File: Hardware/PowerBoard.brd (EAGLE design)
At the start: 97 x 38.1 mm, 32 parts, among them IC1 MAX232, IC2 7805

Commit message: Added HV supply; cleaned up power board
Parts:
- removed C1: 2.2µF, rcl:C0805
- removed C7: 100nF, rcl:C0805
- added C104: 2.2µF, rcl:C0805
- added C106: 100nF, rcl:C0805
- renumbered C10 to C207, C12 to C202, C13 to C206, C2 to C103, C24 to C203, C25 to C204, C26 to C201, C3 to C105, C4 to C107, C5 to C101, C6 to C102, C8 to C205, H1 to H101, H2 to H102, H3 to H103, IC1 to IC101, IC2 to IC201, LED1 to LED201, LED5 to LED202, R1 to R201, R13 to R202, S2 to S101, SV1 to SV202, SV2 to SV203, SV3 to SV204, SV5 to SV101, SV6 to SV102, SV7 to SV201, X1 to X101, X2 to X102
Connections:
- net +5V: now also C106.1; no longer C7.1
- net GND: now also C104.2, C106.2; no longer C1.2, C7.2
- net N$1: now also C104.1; no longer C1.1
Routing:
- net +5V: track 159.9 -> 161.3 mm
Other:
- board text added: "UART/Power Board Rev 01"

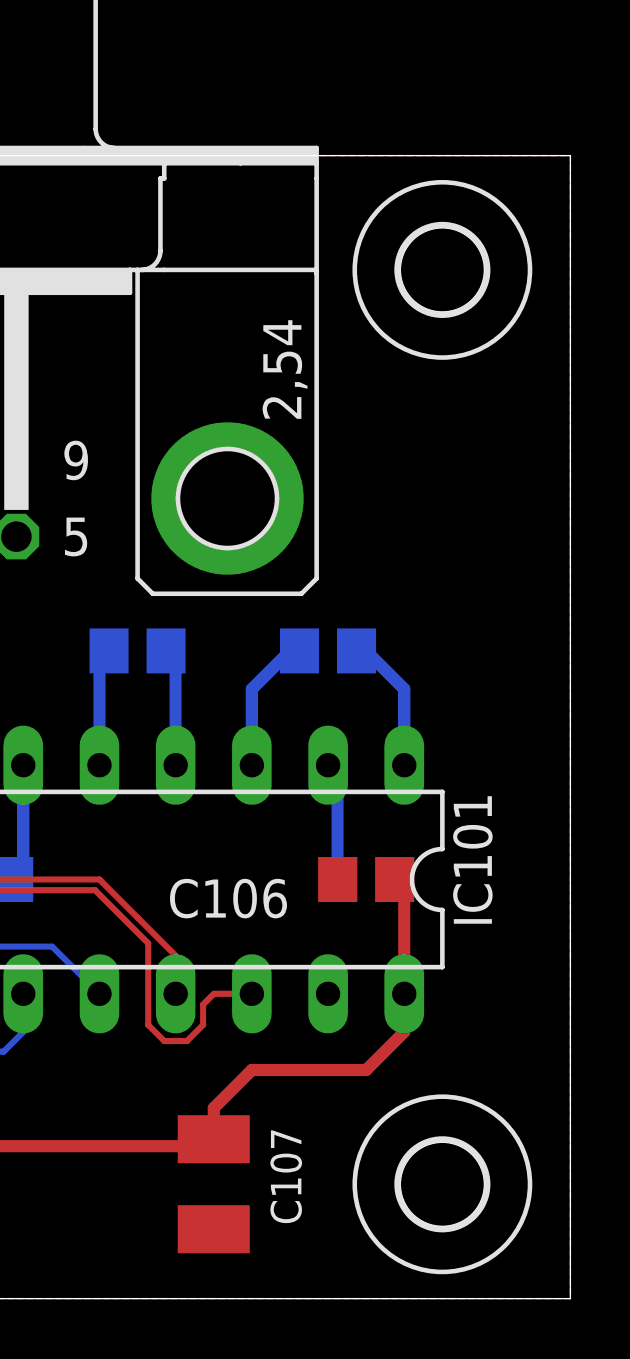
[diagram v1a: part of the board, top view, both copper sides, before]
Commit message: added ARM chip to driver boards to PWM tubes
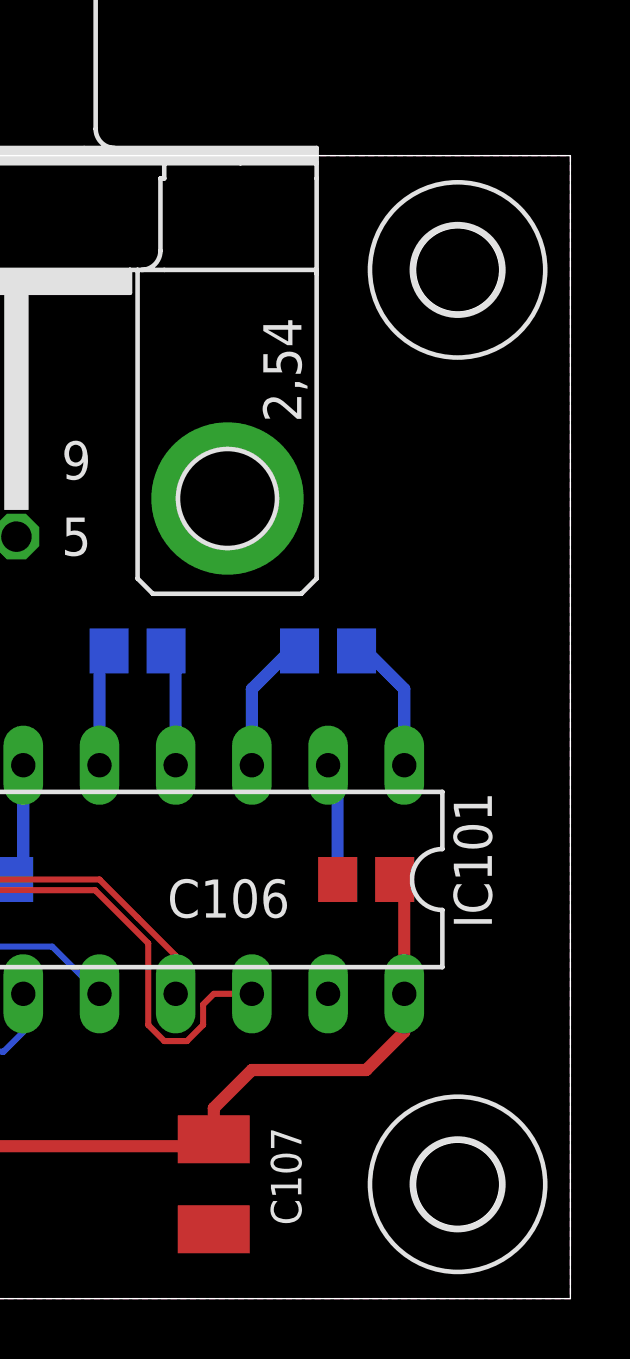
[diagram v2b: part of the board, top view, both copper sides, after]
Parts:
- moved H102 0.51 mm to (93.2, 34.3)
- moved H103 0.51 mm to (93.2, 3.81)
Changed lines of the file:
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@@
 </class>
 </classes>
-<designrules name="default">
-<description language="en">&lt;b&gt;EAGLE Design Rules&lt;/b&gt;
-&lt;p&gt;
-The default Design Rules have been set to cover
-a wide range of applications. Your particular design
-may have different requirements, so please make the
-necessary adjustments and save your customized
-design rules under a new name.
-</description>
+<designrules name="dirt_cheap_dirty_boards.v1.1">
+<description language="de">&lt;b&gt;Dirty Cheap Dirty Board Design Rules&lt;/b&gt;
+&lt;br&gt;
+&lt;br&gt;Min width/Spacing: 6/6mil
+&lt;br&gt;Min diameter of finished hole 12mil</description>
+<description language="en">&lt;b&gt;Dirty Cheap Dirty Board Design Rules&lt;/b&gt;
+&lt;br&gt;
+&lt;br&gt;Min width/Spacing: 6/6mil
+&lt;br&gt;Min diameter of finished hole 12mil</description>
+<description language="zh">&lt;b&gt;Dirty Cheap Dirty Board Design Rules&lt;/b&gt;
+&lt;br&gt;
+&lt;br&gt;Min width/Spacing: 6/6mil
+&lt;br&gt;Min diameter of finished hole 12mil</description>
 <param name="layerSetup" value="(1*16)"/>
-<param name="mtCopper" value="0.035mm 0.035mm 0.035mm 0.035mm 0.035mm 0.035mm 0.035mm 0.035mm 0.035mm 0.035mm 0.035mm 0.035mm 0.035mm 0.035mm 0.035mm 0.035mm"/>
-<param name="mtIsolate" value="0.15mm 0.15mm 0.2mm 0.15mm 0.2mm 0.15mm 0.2mm 0.15mm 0.2mm 0.15mm 0.2mm 0.15mm 0.2mm 0.15mm 0.2mm"/>
+<param name="mtCopper" value="0.035mm 0.0175mm 0.035mm 0.035mm 0.035mm 0.035mm 0.035mm 0.035mm 0.035mm 0.035mm 0.035mm 0.035mm 0.035mm 0.035mm 0.0175mm 0.035mm"/>
+<param name="mtIsolate" value="1.5mm 1.1mm 0.2mm 0.15mm 0.2mm 0.15mm 0.2mm 0.15mm 0.2mm 0.15mm 0.2mm 0.15mm 0.2mm 0.15mm 0.2mm"/>
 <param name="mdWireWire" value="6mil"/>
 <param name="mdWirePad" value="6mil"/>
@@
 <param name="mdPadVia" value="6mil"/>
 <param name="mdViaVia" value="6mil"/>
-<param name="mdSmdPad" value="6mil"/>
-<param name="mdSmdVia" value="6mil"/>
-<param name="mdSmdSmd" value="6mil"/>
-<param name="mdViaViaSameLayer" value="6mil"/>
+<param name="mdSmdPad" value="0mil"/>
+<param name="mdSmdVia" value="0mil"/>
+<param name="mdSmdSmd" value="0mil"/>
+<param name="mdViaViaSameLayer" value="8mil"/>
 <param name="mnLayersViaInSmd" value="2"/>
-<param name="mdCopperDimension" value="40mil"/>
-<param name="mdDrill" value="6mil"/>
+<param name="mdCopperDimension" value="10mil"/>
+<param name="mdDrill" value="10mil"/>
 <param name="mdSmdStop" value="0mil"/>
 <param name="msWidth" value="6mil"/>
-<param name="msDrill" value="0.35mm"/>
-<param name="msMicroVia" value="9.99mm"/>
+<param name="msDrill" value="12mil"/>
+<param name="msMicroVia" value="12mil"/>
 <param name="msBlindViaRatio" value="0.5"/>
 <param name="rvPadTop" value="0.25"/>
@@
 <param name="rlMinPadBottom" value="10mil"/>
 <param name="rlMaxPadBottom" value="20mil"/>
-<param name="rlMinViaOuter" value="8mil"/>
+<param name="rlMinViaOuter" value="6mil"/>
 <param name="rlMaxViaOuter" value="20mil"/>
-<param name="rlMinViaInner" value="8mil"/>
+<param name="rlMinViaInner" value="6mil"/>
 <param name="rlMaxViaInner" value="20mil"/>
 <param name="rlMinMicroViaOuter" value="4mil"/>
@@
 <param name="psTop" value="-1"/>
 <param name="psBottom" value="-1"/>
-<param name="psFirst" value="-1"/>
+<param name="psFirst" value="0"/>
 <param name="psElongationLong" value="100"/>
 <param name="psElongationOffset" value="100"/>
 <param name="mvStopFrame" value="1"/>
 <param name="mvCreamFrame" value="0"/>
-<param name="mlMinStopFrame" value="4mil"/>
-<param name="mlMaxStopFrame" value="4mil"/>
+<param name="mlMinStopFrame" value="2mil"/>
+<param name="mlMaxStopFrame" value="2mil"/>
 <param name="mlMinCreamFrame" value="0mil"/>
 <param name="mlMaxCreamFrame" value="0mil"/>
-<param name="mlViaStopLimit" value="0mil"/>
+<param name="mlViaStopLimit" value="25mil"/>
 <param name="srRoundness" value="0"/>
 <param name="srMinRoundness" value="0mil"/>
@@
 <param name="checkAngle" value="0"/>
 <param name="checkFont" value="1"/>
-<param name="checkRestrict" value="1"/>
+<param name="checkRestrict" value="0"/>
 <param name="checkStop" value="0"/>
 <param name="checkValues" value="0"/>
@@
 <param name="checkPolygonWidth" value="0"/>
 <param name="useDiameter" value="13"/>
-<param name="maxErrors" value="999999"/>
+<param name="maxErrors" value="50"/>
 </designrules>
 <autorouter>
@@
 </element>
 <element name="H101" library="holes" library_urn="urn:adsk.eagle:library:237" package="2,8" package3d_urn="urn:adsk.eagle:package:14271/1" value="MOUNT-HOLE2.8" x="3.81" y="34.29" smashed="yes"/>
-<element name="H102" library="holes" library_urn="urn:adsk.eagle:library:237" package="2,8" package3d_urn="urn:adsk.eagle:package:14271/1" value="MOUNT-HOLE2.8" x="92.71" y="34.29" smashed="yes"/>
-<element name="H103" library="holes" library_urn="urn:adsk.eagle:library:237" package="2,8" package3d_urn="urn:adsk.eagle:package:14271/1" value="MOUNT-HOLE2.8" x="92.71" y="3.81" smashed="yes"/>
+<element name="H102" library="holes" library_urn="urn:adsk.eagle:library:237" package="2,8" package3d_urn="urn:adsk.eagle:package:14271/1" value="MOUNT-HOLE2.8" x="93.218" y="34.29" smashed="yes"/>
+<element name="H103" library="holes" library_urn="urn:adsk.eagle:library:237" package="2,8" package3d_urn="urn:adsk.eagle:package:14271/1" value="MOUNT-HOLE2.8" x="93.218" y="3.81" smashed="yes"/>
 <element name="IC101" library="maxim" library_urn="urn:adsk.eagle:library:269" package="DIL16" package3d_urn="urn:adsk.eagle:package:922/2" value="MAX232" x="82.55" y="13.97" smashed="yes" rot="R180">
 <attribute name="MF" value="MAXIM" x="34.29" y="45.72" size="1.778" layer="27" rot="R180" display="off"/>
